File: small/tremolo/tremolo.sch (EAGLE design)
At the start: 50 parts, among them IC1 NE5532, IC2 PT2399, Q1 J112

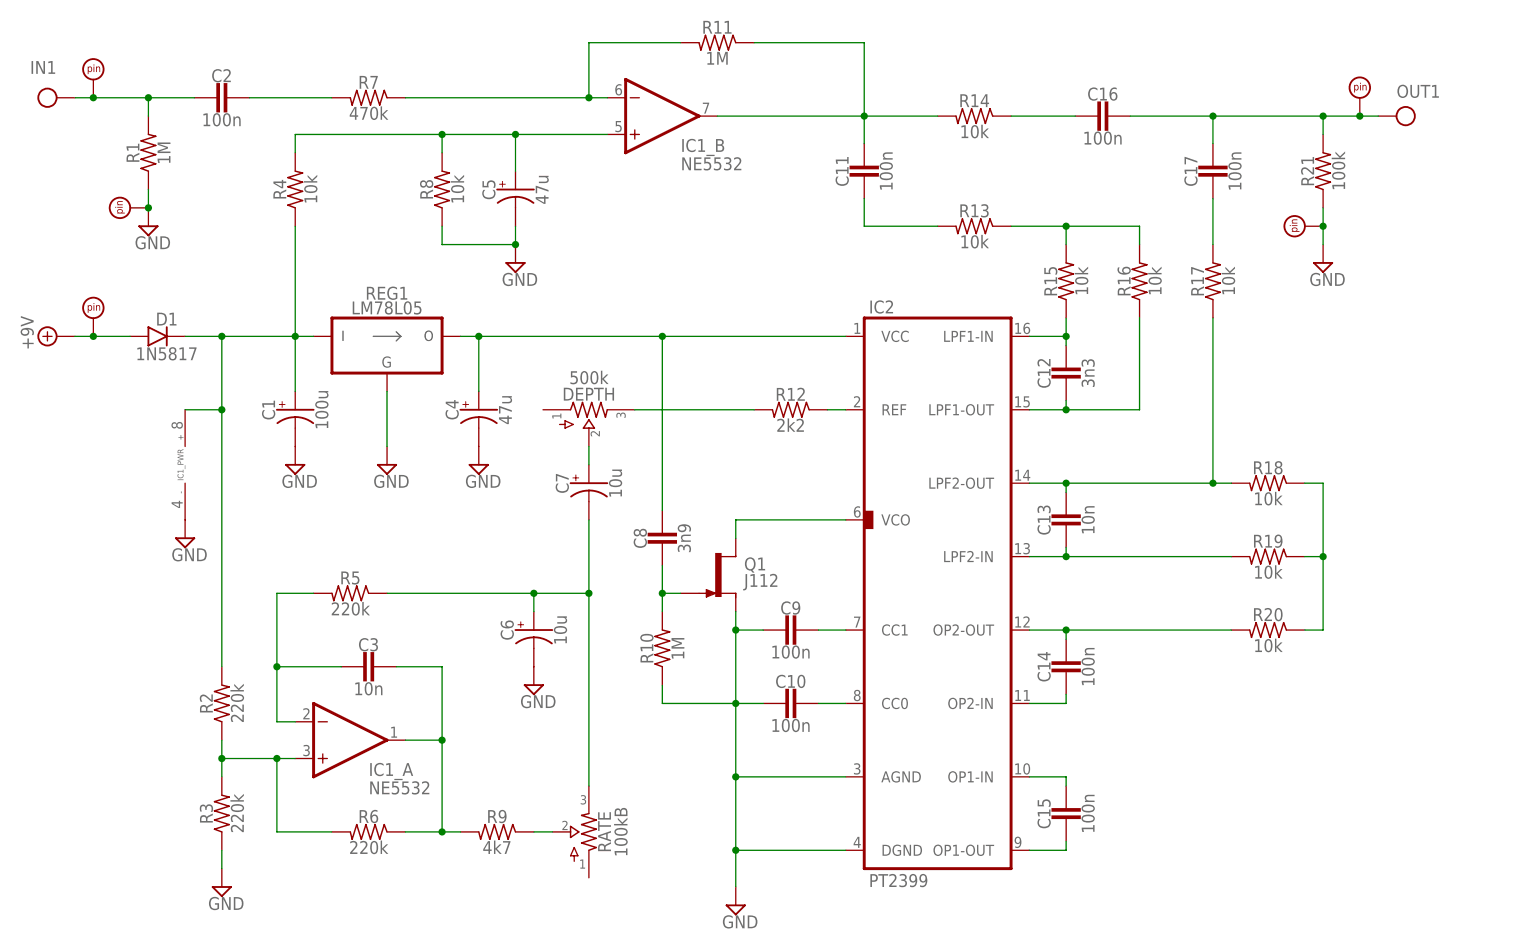
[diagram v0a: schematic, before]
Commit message: add beginnings of tremolo; minor copy tweaks to other schems
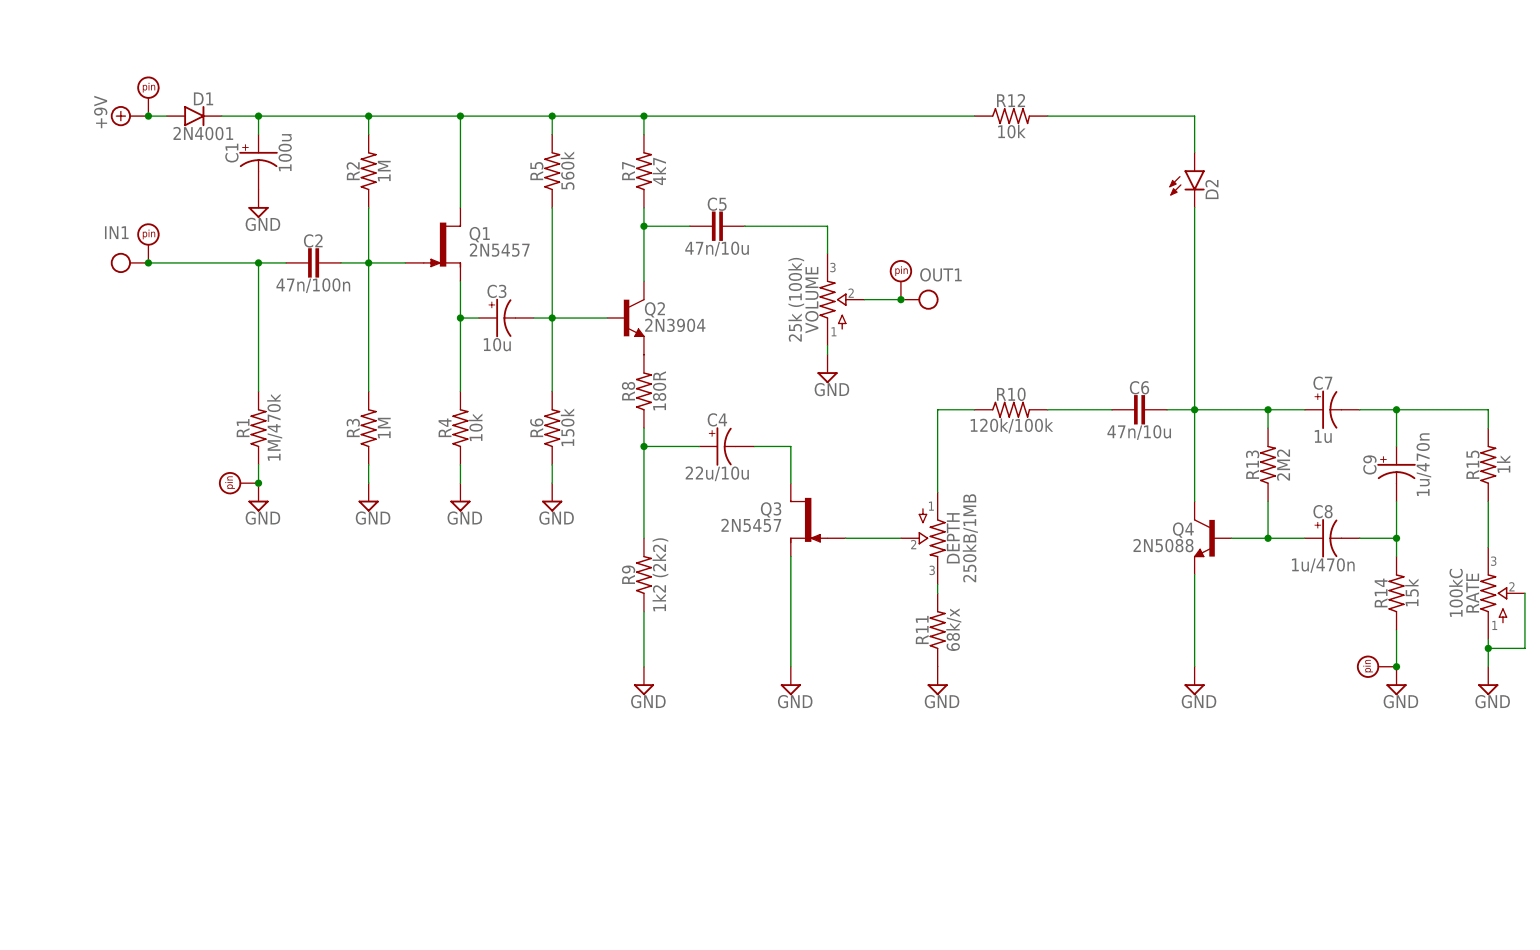
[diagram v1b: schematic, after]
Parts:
- removed C10, C11, C14, C15, C16, C17: 100n, capacitors-film:CER/FILMBOX.1
- removed C12: 3n3, capacitors-film:CER/FILMBOX.1
- removed C13: 10n, capacitors-film:CER/FILMBOX.1
- removed IC1: NE5532, integrated circuits:DUALTH
- removed IC2: PT2399, integrated circuits:PT2399TH
- removed R16, R17, R18, R19, R20: 10k, resistors:R_.2
- removed R21: 100k, resistors:R_.2
- removed REG1: LM78L05, regulators:LM78L05
- added D2: LEDA, diodes:LEDA
- added Q2: 2N3904, transistors:2N3904
- added Q3: 2N5457, transistors:2N5457
- added Q4: 2N5088, transistors:2N5088
- added VOLUME: 25k (100k), potentiometers:POTSTRIM
- C2: value 100n -> 47n/100n
- C3: value 10n -> 10u; device capacitors-film:CER/FILMBOX.1 -> capacitors-elec:0501
- C4: value 47u -> 22u/10u
- C5: value 47u -> 47n/10u; device capacitors-elec:0501 -> capacitors-film:CER/FILMBOX.1
- C6: value 10u -> 47n/10u; device capacitors-elec:0501 -> capacitors-film:CER/FILMBOX.1
- C7: value 10u -> 1u
- C8: value 3n9 -> 1u/470n; device capacitors-film:CER/FILMBOX.1 -> capacitors-elec:0501
- C9: value 100n -> 1u/470n; device capacitors-film:CER/FILMBOX.1 -> capacitors-elec:0501
- D1: value 1N5817 -> 2N4001
- DEPTH: value 500k -> 250kB/1MB; device potentiometers:POTSTRIM -> potentiometers:POTSSMALL_PADS
- PAD3: value PADRND -> PADSQR; device supply pins:PADRND -> supply pins:PADSQR
- PAD5: value PADSQR -> PADRND; device supply pins:PADSQR -> supply pins:PADRND
- Q1: value J112 -> 2N5457
- R1: value 1M -> 1M/470k; device resistors:R_.2 -> resistors:R_.3B
- R10: value 1M -> 120k/100k; device resistors:R_.2 -> resistors:R_.3B
- R11: value 1M -> 68k/x; device resistors:R_.2 -> resistors:R_.3B
- R12: value 2k2 -> 10k; device resistors:R_.2 -> resistors:R_.3B
- R13: value 10k -> 2M2; device resistors:R_.2 -> resistors:R_.3B
- R14: value 10k -> 15k; device resistors:R_.2 -> resistors:R_.3B
- R15: value 10k -> 1k; device resistors:R_.2 -> resistors:R_.3B
- R2, R3: value 220k -> 1M; device resistors:R_.2 -> resistors:R_.3B
- R4: device resistors:R_.2 -> resistors:R_.3B
- R5: value 220k -> 560k; device resistors:R_.2 -> resistors:R_.3B
- R6: value 220k -> 150k; device resistors:R_.2 -> resistors:R_.3B
- R7: value 470k -> 4k7; device resistors:R_.2 -> resistors:R_.3B
- R8: value 10k -> 180R; device resistors:R_.2 -> resistors:R_.3B
- R9: value 4k7 -> 1k2 (2k2); device resistors:R_.2 -> resistors:R_.3B
- RATE: value 100kB -> 100kC
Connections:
- removed net N$20: IC2.REF, R12.1
- removed net N$21: IC2.VCO, Q1.D
- removed net N$22: C7.+, DEPTH.2
- removed net N$23: C9.1, IC2.CC1
- removed net N$24: C10.1, IC2.CC0
- removed net N$25: IC1_A.+IN, R2.1, R3.2, R6.2
- removed net N$26: C3.2, IC1_A.-IN, R5.2
- removed net N$28: C6.+, C7.-, R5.1, RATE.3
- removed net N$29: R9.1, RATE.2
- removed net N$30: C3.1, IC1_A.OUT, R6.1, R9.2
- removed net N$31: C8.2, Q1.G, R10.2
- removed net N$32: C1.+, D1.C, IC1_PWR.V+, R2.2, R4.1, REG1.VI
- net +9V: now also PAD1.P$1; no longer PAD2.P$1
- net GND: now also PAD5.P$1, Q3.S, Q4.E, R11.1, R14.1, R4.1, R6.1, R9.1, RATE.1, RATE.2, VOLUME.1; no longer C10.2, C4.-, C5.-, C6.-, C9.2, IC1_PWR.V-, IC2.AGND, IC2.DGND, PAD3.P$1, Q1.S, R10.1, R21.1, R8.1, REG1.GND
- net IN: now also PAD2.P$1; no longer PAD1.P$1
- net N$1: now also C2.1, Q1.G, R2.1, R3.2; no longer C12.1, IC2.LPF1-IN, R15.1
- net N$10: now also DEPTH.2, Q3.G; no longer C15.1, IC2.OP1-IN
- net N$11: now also DEPTH.1, R10.1; no longer C15.2, IC2.OP1-OUT
- net N$12: now also C6.2, R10.2; no longer C17.2, R17.2
- net N$13: now also C6.1, C7.+, D2.C, Q4.C, R13.2; no longer C16.2, R14.1
- net N$14: now also C8.+, Q4.B, R13.1; no longer C11.1, IC1_B.OUT, R11.1, R14.2
- net N$15: now also C7.-, C9.+, R15.2; no longer IC1_B.-IN, R11.2, R7.1
- net N$16: now also C8.-, C9.-, R14.2; no longer C2.1, R7.2
- net N$17: now also DEPTH.3, R11.2; no longer C11.2, R13.2
- net N$18: now also R15.1, RATE.3; no longer C5.+, IC1_B.+IN, R4.2, R8.2
- net N$19: now also D2.A, R12.2; no longer C4.+, C8.1, IC2.VCC, REG1.VO
- net N$2: now also C3.+, Q1.S, R4.2; no longer C12.2, IC2.LPF1-OUT, R16.1
- net N$3: now also C3.-, Q2.B, R5.1, R6.2; no longer DEPTH.3, R12.2
- net N$4: now also C5.2, Q2.C, R7.1; no longer R13.1, R15.2, R16.2
- net N$5: now also Q2.E, R8.2; no longer C13.1, IC2.LPF2-OUT, R17.1, R18.2
- net N$6: now also C5.1, VOLUME.3; no longer C14.1, IC2.OP2-OUT, R20.2
- net N$7: now also C1.+, D1.C, Q1.D, R12.1, R2.2, R5.2, R7.2; no longer C13.2, IC2.LPF2-IN, R19.2
- net N$8: now also C4.+, R8.1, R9.2; no longer R18.1, R19.1, R20.1
- net N$9: now also C4.-, Q3.D; no longer C14.2, IC2.OP2-IN
- net OUT: now also PAD3.P$1, VOLUME.2; no longer C16.1, C17.1, PAD5.P$1, R21.2
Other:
- moved on the sheet: C1, C2, C4, C7, D1, DEPTH, Q1, R1, R10, R11, R12, R13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
